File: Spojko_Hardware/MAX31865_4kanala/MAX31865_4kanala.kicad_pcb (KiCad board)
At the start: 2 copper layers, 139.7 x 63.5 mm, 42 parts, among them J1 CONN_01X04, J10 CONN_01X04, J11 CONN_01X04, J12 CONN_01X04, J13 CONN_01X04, J2 CONN_01X04, J3 CONN_01X04, J4 CONN_01X04, J5 CONN_01X40, U1 MAX31865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

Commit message: Ponovno rutovanje i izbacivanje konektora...
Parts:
- removed C13: 4.7uF 25V, Capacitors_SMD:C_1206
- removed J10, J11, J12, J13: CONN_01X04, Pin_Headers:Pin_Header_Straight_1x04_Pitch2.54mm
- C1, C2, C3, C4: footprint Capacitors_SMD:C_1206 -> Capacitors_SMD:C_0805
- C10, C11, C12, C9: footprint Capacitors_Tantalum_SMD:CP_Tantalum_Case-B_EIA-3528-21_Hand -> Capacitors_SMD:C_0805
- C5, C6, C7, C8: footprint Capacitors_SMD:C_0805_HandSoldering -> Capacitors_SMD:C_0805
- moved C12 83.3 mm to (189.5, 89.0)
- moved C8 76.8 mm to (185.9, 89.0)
- moved C7 35.3 mm to (159.9, 89.3), turned to 270 degrees
- moved C5 27.8 mm to (120.4, 89.3), turned to 270 degrees
- moved C6 27.6 mm to (140.3, 89.3), turned to 270 degrees
- moved C10 24.3 mm to (143.9, 89.3), turned to 270 degrees
- moved C9 21.3 mm to (123.8, 89.2), turned to 270 degrees
- moved J4 11.4 mm to (174.9, 73.9)
- moved C11 10.5 mm to (163.4, 89.3), turned to 270 degrees
- moved R12 10.0 mm to (131.4, 95.9)
- moved R11 9.92 mm to (111.1, 96.0)
- moved R9 9.50 mm to (150.6, 96.1)
- moved R10 9.21 mm to (175.8, 96.1)
- moved R7 5.48 mm to (180.6, 95.2)
- moved R4 5.30 mm to (180.3, 84.1)
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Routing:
- net CS3: track 91.1 -> 0.00 mm, vias 2 -> 0
- net VDD: track 85.0 -> 5.51 mm, vias 4 -> 0
- net CS2: track 74.6 -> 2.41 mm, vias 1 -> 0
- net CS1: track 56.6 -> 0.13 mm, vias 2 -> 0
- net Net-(R13-Pad2): track 48.9 -> 0.36 mm, vias 4 -> 0
- net GND: track 49.5 -> 11.0 mm, vias 2 -> 0
- net /FORCE0-: track 0.12 -> 24.9 mm
- net /FORCE3-: track 23.7 -> 0.00 mm
- net Net-(R14-Pad2): track 23.2 -> 0.12 mm, vias 2 -> 0
- net /RTDIN0-: track 0.00 -> 22.6 mm, vias 0 -> 2
- net Net-(R15-Pad2): track 22.3 -> 0.21 mm, vias 2 -> 0
- net /IFORCE3+: track 19.2 -> 0.00 mm
- net /RTDIN0+: track 0.00 -> 18.8 mm
- net /IFORCE0+: track 0.00 -> 15.0 mm
- net Net-(R6-Pad2): track 13.6 -> 0.13 mm
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- removed copper zone on B.Cu, net GND

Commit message: Izmene predlozi matori
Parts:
- J1, J2, J3, J4: value CONN_01X04 -> 1824763; footprint Socket_Strips:Socket_Strip_Straight_1x04_Pitch2.54mm -> 1824763
- moved J3 22.9 mm to (167.6, 68.6), turned to 180 degrees
- moved J2 19.4 mm to (144.8, 68.6), turned to 180 degrees
- moved J4 16.5 mm to (190.5, 68.6), turned to 180 degrees
- moved J1 14.9 mm to (121.9, 68.6), turned to 180 degrees
- moved C4 11.7 mm to (172.5, 92.7)
- moved R3 6.26 mm to (155.6, 88.8)
- moved U4 6.19 mm to (179.3, 94.2)
- moved C12 5.11 mm to (189.0, 94.1)
- moved C8 5.11 mm to (185.4, 94.1)
- moved R10 5.11 mm to (175.3, 101.2)
- moved R7 5.11 mm to (180.1, 100.3)
- moved R4 5.09 mm to (180.6, 89.2)
- moved C1 4.89 mm to (108.7, 92.5)
- moved C9 4.89 mm to (124.6, 94.0)
- moved R5 4.89 mm to (136.4, 99.8)
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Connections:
- J1 pad 3: /RTDIN0- -> /FORCE0-
- J1 pad 4: /FORCE0- -> /RTDIN0-
- J2 pad 3: /RTDIN1- -> /FORCE1-
- J2 pad 4: /FORCE1- -> /RTDIN1-
- J3 pad 3: /RTDIN2- -> /FORCE2-
- J3 pad 4: /FORCE2- -> /RTDIN2-
- J4 pad 3: /RTDIN3- -> /FORCE3-
- J4 pad 4: /FORCE3- -> /RTDIN3-
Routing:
- net VCC: track 0.50 -> 99.1 mm, vias 0 -> 2
- net CS3: track 0.00 -> 96.8 mm, vias 0 -> 1
- net Net-(R13-Pad2): track 0.36 -> 89.6 mm, vias 0 -> 8
- net CS2: track 2.41 -> 76.7 mm, vias 0 -> 2
- net VDD: track 5.51 -> 76.8 mm, vias 0 -> 4
- net CS1: track 0.13 -> 57.9 mm, vias 0 -> 1
- net Net-(R15-Pad2): track 0.21 -> 44.5 mm, vias 0 -> 4
- net CS0: track 0.14 -> 40.1 mm, vias 0 -> 1
- net Net-(R14-Pad2): track 0.12 -> 39.5 mm, vias 0 -> 4
- net /FORCE0-: track 24.9 -> 0.00 mm
- net GND: track 11.0 -> 32.1 mm, vias 0 -> 2
- net /IFORCE3+: track 0.00 -> 18.7 mm, vias 0 -> 2
- net /FORCE3-: track 0.00 -> 16.0 mm, vias 0 -> 2
- net /FORCE2-: track 0.00 -> 15.8 mm, vias 0 -> 2
- net /RTDIN0+: track 18.8 -> 3.37 mm
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
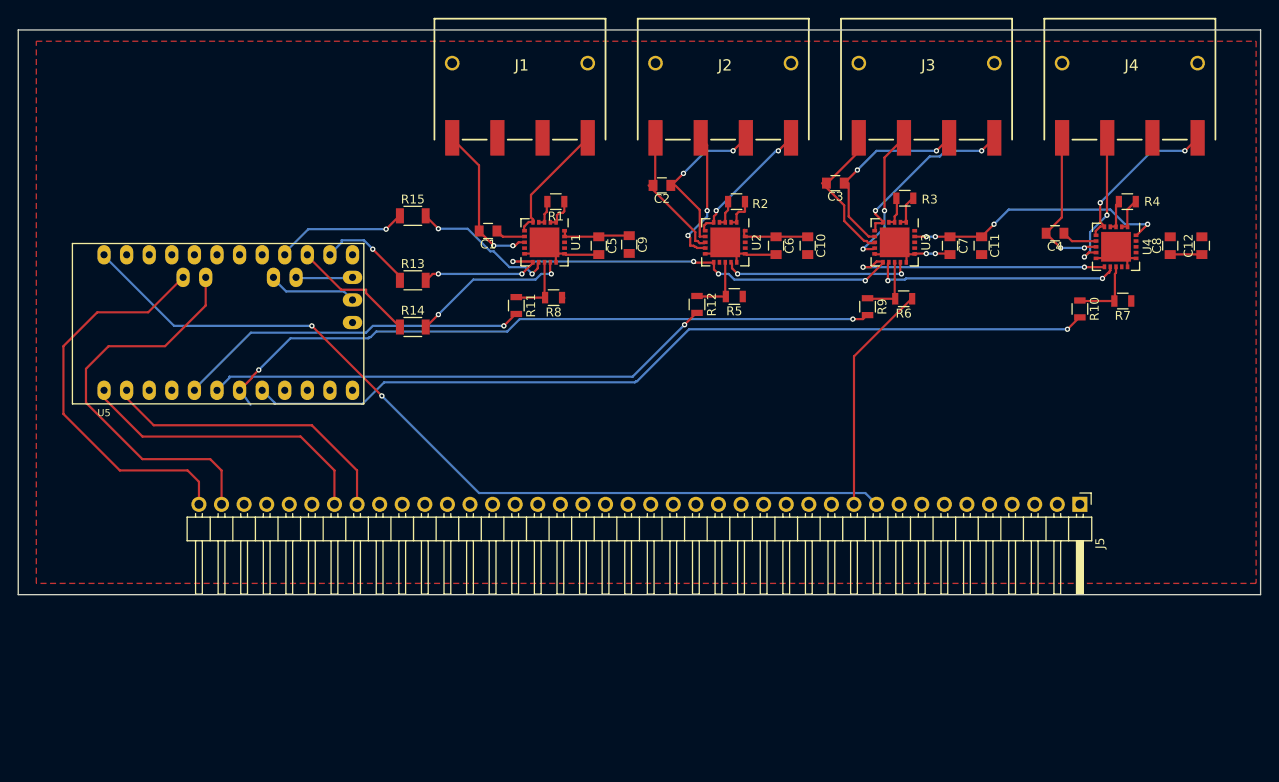
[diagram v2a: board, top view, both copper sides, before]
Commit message: Added gif main ReadMe
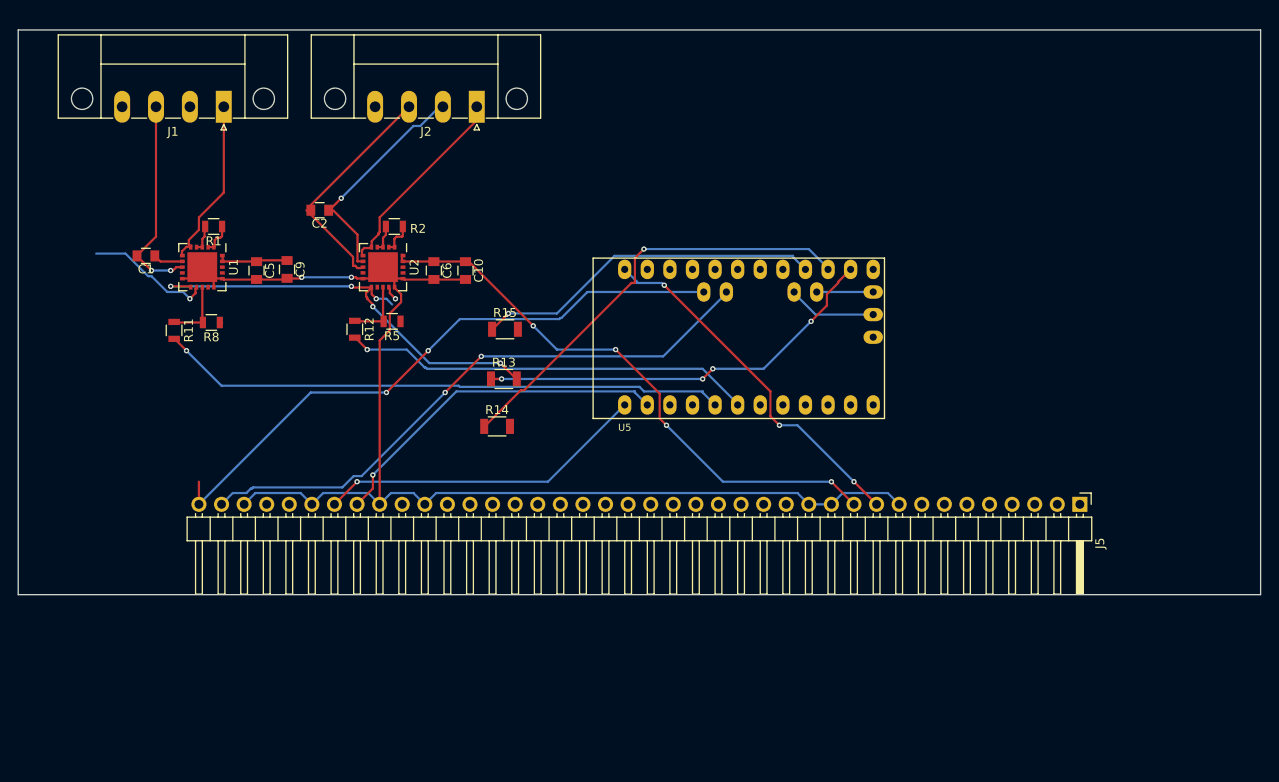
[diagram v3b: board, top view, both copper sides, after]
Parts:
- removed C11, C12, C7, C8: C, Capacitors_SMD:C_0805
- removed C3, C4: 0.1uF 25V, X7R, Capacitors_SMD:C_0805
- removed J3, J4: 1824763, 1824763
- removed R10, R6, R7, R9: 150, Resistors_SMD:R_0805
- removed R3, R4: 400, Resistors_SMD:R_0805
- removed U3, U4: MAX31865, project_footprints:QFN-20-1EP_5x5mm_Pitch0.65mm
- J1, J2: value 1824763 -> CONN_01X04; footprint 1824763 -> Connectors_Phoenix:PhoenixContact_MC-GF_04x3.81mm_Angled_ThreadedFlange_MountHole
- moved U5 58.6 mm to (138.0, 104.4)
- moved J1 44.1 mm to (79.0, 78.5)
- moved J2 38.6 mm to (107.4, 78.5)
- moved C1 38.6 mm to (70.2, 95.2)
- moved C6 38.6 mm to (102.6, 96.9)
- moved C9 38.6 mm to (86.1, 96.8)
- moved R8 38.6 mm to (77.6, 102.7)
- moved U2 38.6 mm to (96.9, 96.5)
- moved C10 38.6 mm to (106.2, 96.9)
- moved C2 38.6 mm to (89.8, 90.1)
- moved C5 38.6 mm to (82.7, 96.9)
- moved R1 38.6 mm to (77.9, 91.9)
- moved R11 38.6 mm to (73.4, 103.6)
- moved R12 38.6 mm to (93.7, 103.5)
- moved R5 38.6 mm to (97.9, 102.6)
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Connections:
- J1 pad 3: /FORCE0- -> /RTDIN0-
- J1 pad 4: /RTDIN0- -> /FORCE0-
- J2 pad 3: /FORCE1- -> /RTDIN1-
- J2 pad 4: /RTDIN1- -> /FORCE1-
- U5 pad 7: CS2 -> DO0
- U5 pad 8: CS3 -> DO1
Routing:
- net GND: track 32.1 -> 149.5 mm
- net CS3: track 96.8 -> 0.00 mm, vias 1 -> 0
- net CS2: track 76.7 -> 0.00 mm, vias 2 -> 0
- net VCC: track 99.1 -> 41.1 mm, vias 2 -> 3
- net Net-(R13-Pad2): track 89.6 -> 51.1 mm, vias 8 -> 5
- net Net-(R14-Pad2): track 39.5 -> 1.66 mm, vias 4 -> 1
- net Net-(R14-Pad1): track 14.1 -> 49.6 mm, vias 0 -> 1
- net Net-(R13-Pad1): track 11.1 -> 46.4 mm, vias 1 -> 4
- net Net-(R15-Pad2): track 44.5 -> 14.3 mm, vias 4 -> 1
- net Net-(R15-Pad1): track 15.2 -> 39.4 mm
- net CS0: track 40.1 -> 64.1 mm
- net SCL: track 45.2 -> 69.2 mm, vias 0 -> 2
- net /RTDIN2+: track 21.7 -> 0.00 mm, vias 2 -> 0
- net SDA: track 45.9 -> 66.7 mm, vias 0 -> 2
- net /IFORCE2+: track 20.4 -> 0.00 mm, vias 2 -> 0
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- removed copper zone on F.Cu, net GND
